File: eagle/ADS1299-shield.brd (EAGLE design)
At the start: 101.6 x 53.3 mm, 125 parts, among them IC1 ADS1299IPAG, IC2 TPS72325DBVT, IC3 TPS73225DBVT, IC5 24AA256UID, IC6 TPS604XXDBV, IC7 OPA376DBV, IC8 OPA376DBV, J8 Electrode Connector, U2 TXB0108PWR, U3 TXB0108PWR

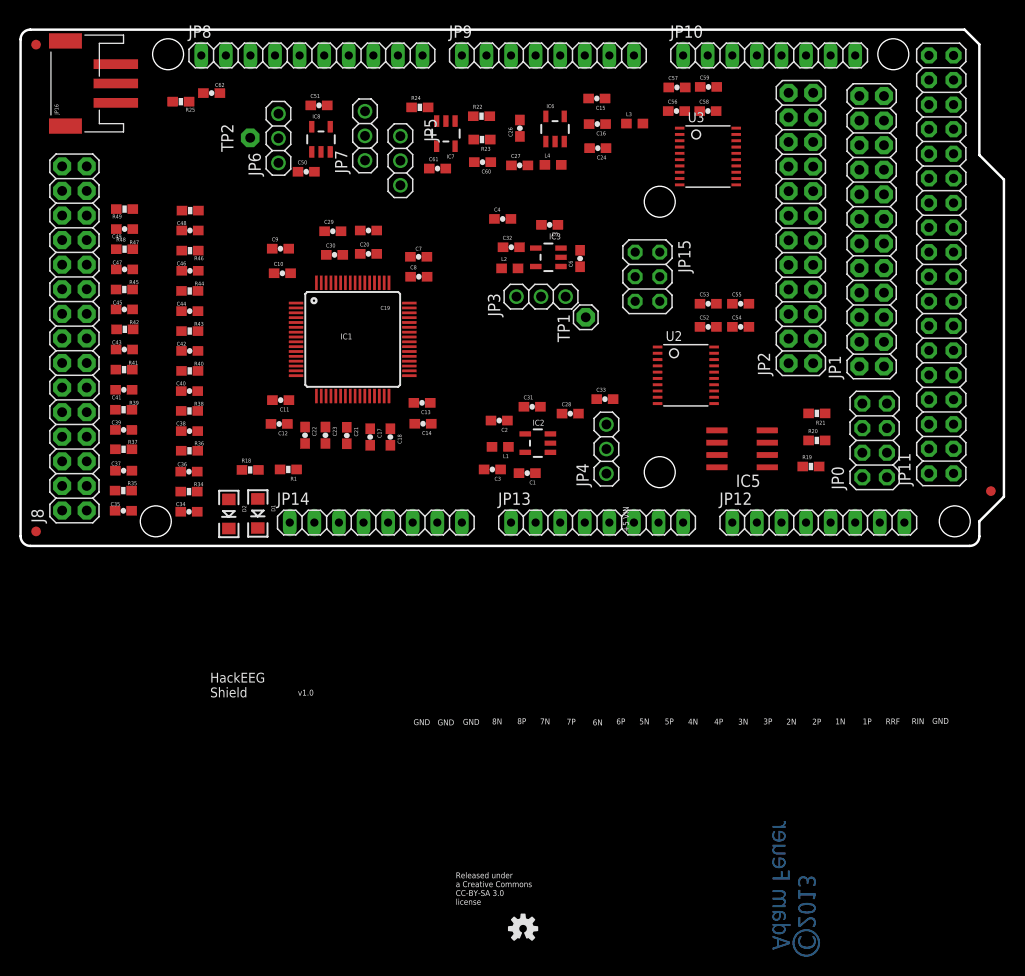
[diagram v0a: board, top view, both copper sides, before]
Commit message: new component arrangement - AIN block neat; configuration blocks moved to make more space for routing
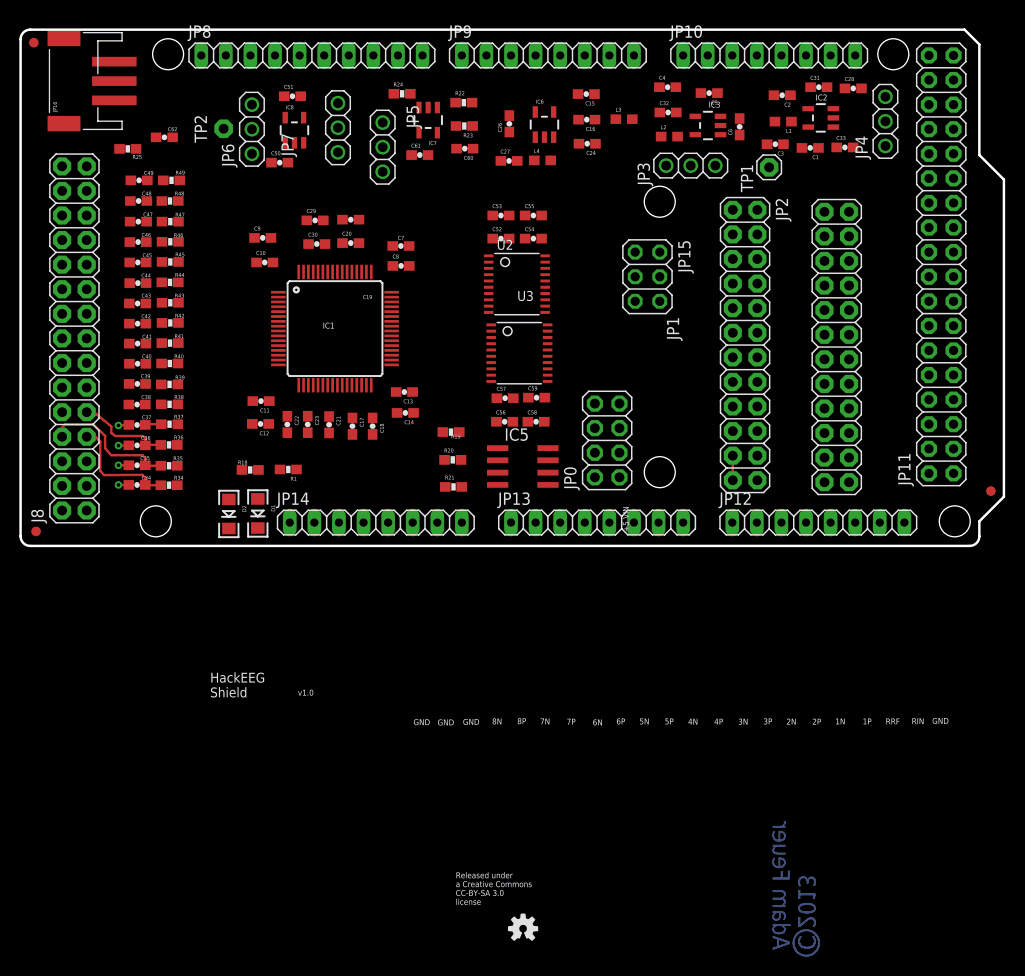
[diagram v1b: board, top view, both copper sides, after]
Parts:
- moved C2 44.5 mm to (78.8, 46.7)
- moved C28 44.5 mm to (86.2, 47.4)
- moved C3 44.5 mm to (78.1, 41.6)
- moved C1 44.5 mm to (81.7, 41.2)
- moved IC2 44.5 mm to (82.8, 44.3)
- moved L1 44.5 mm to (78.9, 44.0)
- moved JP4 44.5 mm to (89.5, 44.0)
- moved C31 44.4 mm to (82.6, 47.5)
- moved R21 38.3 mm to (44.9, 6.22), turned to 0 degrees
- moved R20 37.7 mm to (44.8, 9.02)
- moved R19 37.4 mm to (44.6, 11.9), turned to 180 degrees
- moved C59 36.7 mm to (53.4, 15.4)
- moved C56 36.7 mm to (50.1, 13.0)
- moved C57 36.7 mm to (50.2, 15.4)
- moved C58 36.7 mm to (53.4, 13.0)
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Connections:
- new net N$551: JP2.1, JP2.3
- new net N$552: JP2.2
- new net N$553: JP2.4
- net !ADC_RESET_0: no longer JP2.22
- net !ADC_RESET_1: no longer JP2.24
- net !ADS_SPI_CS: now also U2.15; no longer U2.18
- net !RESET: no longer JP2.21, JP2.23
- net !SPI_CS: now also U2.6; no longer U2.3
- net ADS_CLKSEL: now also U2.20; no longer U2.14
- net ADS_DRDY: now also U2.18; no longer U2.20
- net ADS_SPI_CLK: now also U2.16; no longer U2.17
- net ADS_SPI_IN: now also JP2.21, JP2.23, U2.14; no longer JP2.1, JP2.3, U2.16
- net ADS_SPI_OUT: now also U2.17; no longer U2.15
- net CLKSEL: now also U2.1; no longer U2.7
- net DRDY: now also U2.3; no longer U2.1
- net SPI0_MOSI: now also JP2.22; no longer JP2.2
- net SPI0_SCK: now also JP2.12; no longer JP2.10
- net SPI_CLK: now also U2.5; no longer U2.4
- net SPI_IN: now also U2.7; no longer U2.5
- net SPI_OUT: now also U2.4; no longer U2.6
- net USART1_MOSI: now also JP2.24; no longer JP2.4
- net USART1_SCK: now also JP2.10; no longer JP2.12
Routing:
- net AIN1N: track 0.00 -> 14.6 mm
- net AIN1P: track 0.00 -> 12.0 mm
- net AIN2P: track 0.00 -> 11.2 mm
- net AGND: track 0.00 -> 10.5 mm, vias 0 -> 4
- net ADS_SPI_IN: track 0.00 -> 2.54 mm
- net AIN2N: track 0.00 -> 2.05 mm
- added copper zone on layer 2, net AGND
- added copper zone on layer 15, net DVDD
- removed copper zone on layer 2, net N$22
- removed copper zone on layer 15, net N$25

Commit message: AIN block fully routed
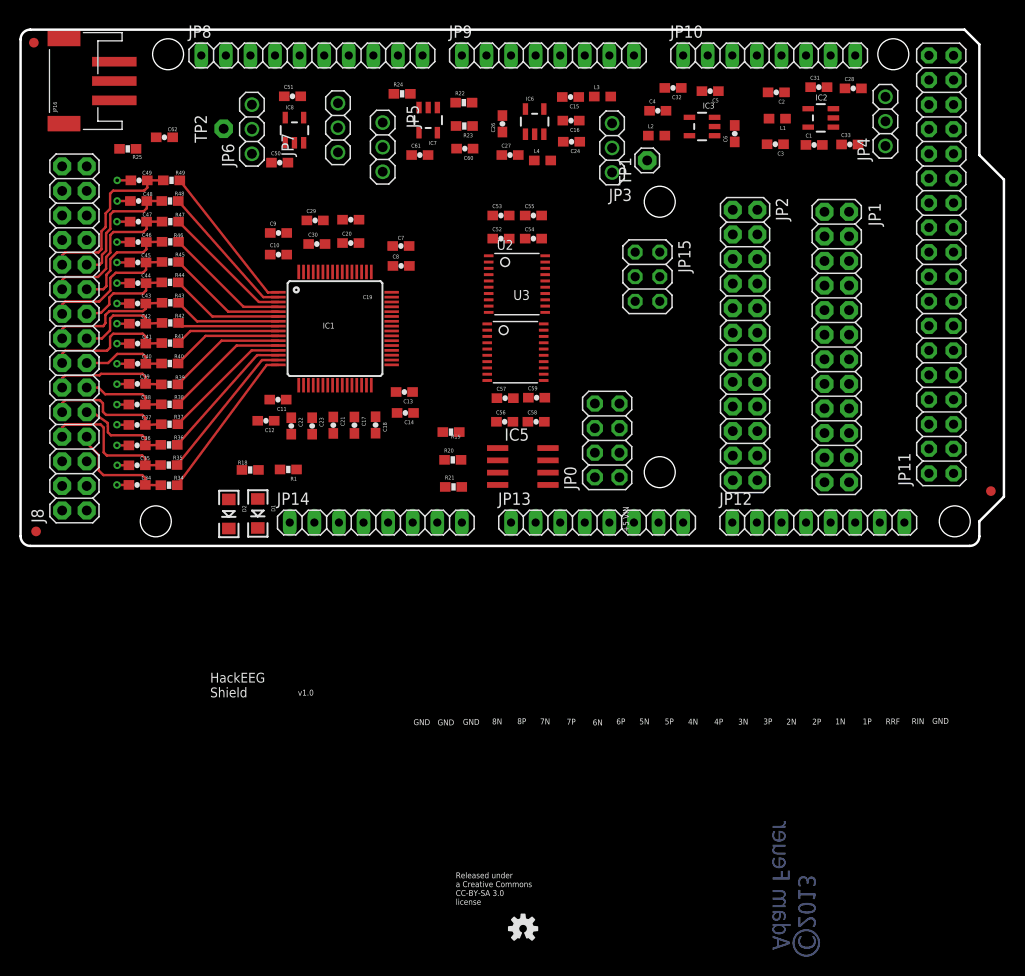
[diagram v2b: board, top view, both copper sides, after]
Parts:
- moved TP1 12.6 mm to (64.9, 40.0)
- moved JP3 8.33 mm to (61.2, 41.2), turned to 90 degrees
- moved L3 3.23 mm to (60.2, 46.6)
- moved C4 2.64 mm to (66.0, 45.1)
- moved C32 2.59 mm to (67.5, 47.4), turned to 180 degrees
- moved C11 1.76 mm to (26.7, 15.2)
- moved C9 1.70 mm to (26.8, 32.5)
- moved C15 1.65 mm to (56.9, 46.5)
- moved C10 1.64 mm to (26.8, 30.2)
- moved C24 1.64 mm to (57.0, 41.9)
- moved C16 1.63 mm to (57.0, 44.1)
- moved L2 1.32 mm to (65.8, 42.5)
- moved IC6 1.06 mm to (53.2, 44.0)
- moved C6 0.87 mm to (73.9, 42.7)
- moved C26 0.71 mm to (49.9, 43.7)
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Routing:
- net AGND: track 10.5 -> 52.5 mm, vias 4 -> 16
- net AIN8N: track 0.00 -> 17.9 mm
- net IN1P: track 0.00 -> 16.7 mm
- net AIN7N: track 0.00 -> 16.0 mm
- net IN8N: track 0.00 -> 15.8 mm
- net IN1N: track 0.00 -> 15.6 mm
- net IN8P: track 0.00 -> 14.8 mm
- net IN2P: track 0.00 -> 14.6 mm
- net AIN6N: track 0.00 -> 14.3 mm
- net IN7N: track 0.00 -> 13.8 mm
- net AIN4N: track 0.00 -> 13.6 mm
- net IN2N: track 0.00 -> 13.6 mm
- net AIN8P: track 0.00 -> 13.3 mm
- net AIN5N: track 0.00 -> 13.2 mm
- net IN7P: track 0.00 -> 13.1 mm
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
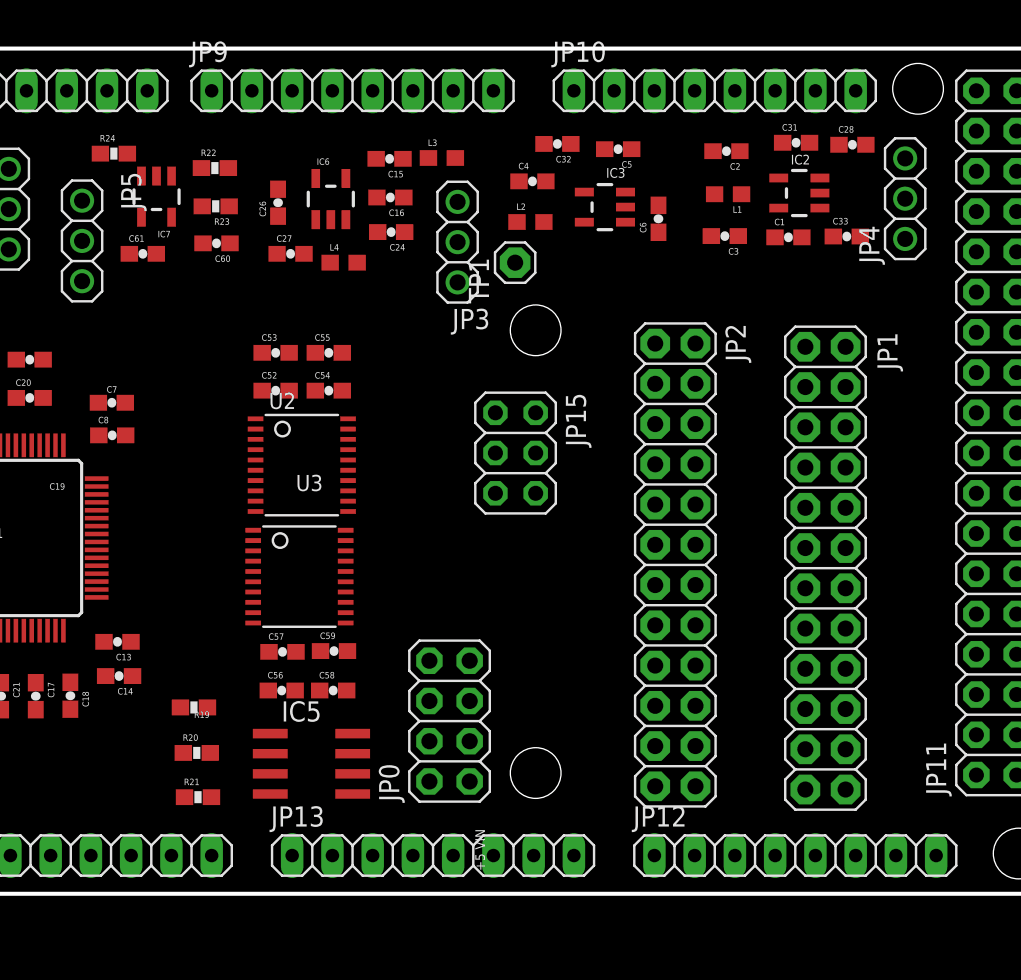
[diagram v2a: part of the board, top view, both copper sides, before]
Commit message: updated 2X10 and 2X12 headers to use smaller pads that can route 2 8mil traces between them; routed SPI MOSI, MISO, and CLK to header pins
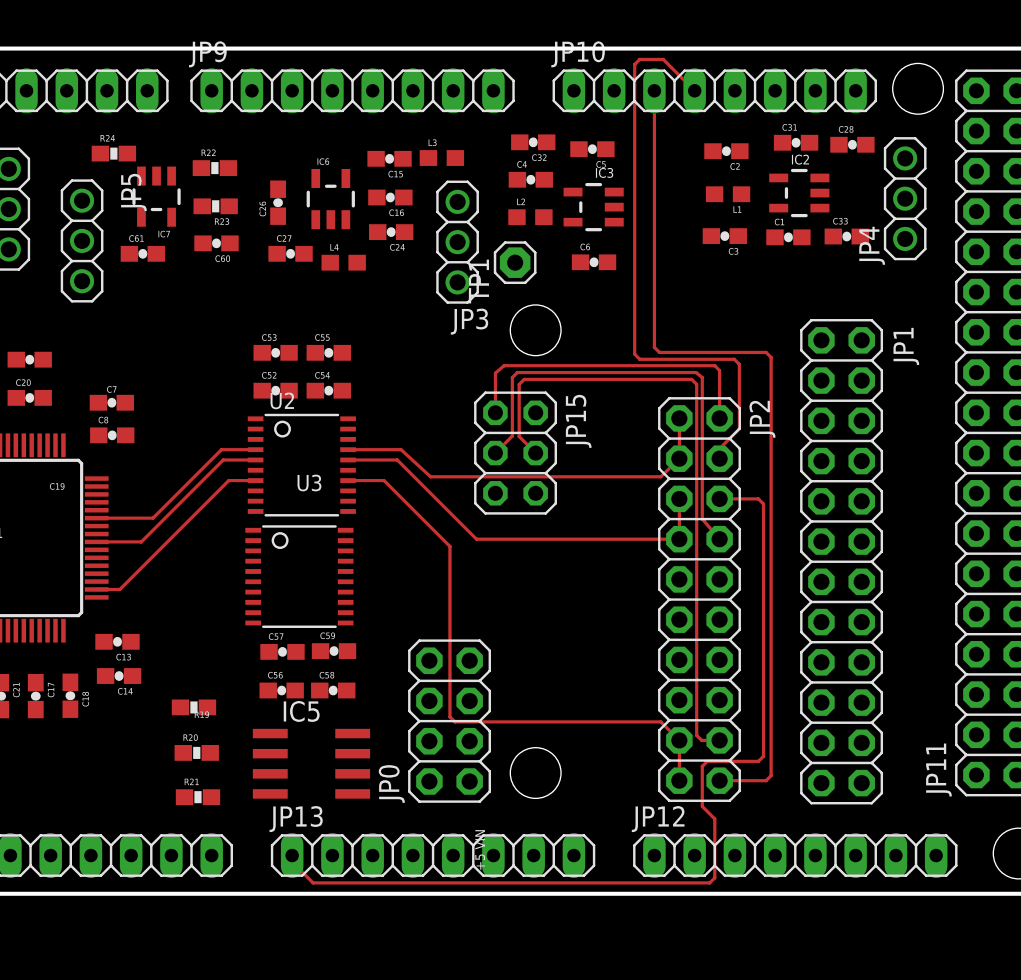
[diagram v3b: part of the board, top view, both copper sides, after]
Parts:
- JP2: value CONFIG2 -> CONFIG3; device pin-headers:2X12 -> headers:2X10
- moved JP2 5.33 mm to (76.5, 18.7)
- moved C6 4.90 mm to (69.8, 40.0), turned to 0 degrees
- moved C5 1.63 mm to (69.7, 47.1)
- moved C32 1.53 mm to (66.0, 47.5)
- moved JP1 1.09 mm to (88.0, 19.8)
- moved IC3 0.71 mm to (69.8, 43.5)
- moved L2 0.30 mm to (65.8, 42.8)
- moved C4 0.14 mm to (65.9, 45.2)
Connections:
- removed net N$551: JP2.1, JP2.3
- removed net N$552: JP2.2
- removed net N$553: JP2.4
- net !ADC_CS_0: now also JP2.10; no longer JP2.14
- net !ADC_CS_1: now also JP2.12; no longer JP2.16
- net !ADC_CS_2: now also JP2.14; no longer JP2.18
- net !ADC_CS_3: now also JP2.16; no longer JP2.20
- net !ADS_SPI_CS: now also JP2.11, JP2.9; no longer JP2.17, JP2.19
- net ADS_SPI_CLK: now also JP2.5, JP2.7; no longer JP2.11, JP2.9
- net ADS_SPI_IN: now also JP2.17, JP2.19; no longer JP2.21, JP2.23
- net ADS_SPI_OUT: now also JP2.1, JP2.3; no longer JP2.5, JP2.7
- net SPI0_MISO: now also JP2.2; no longer JP2.6
- net SPI0_MOSI: now also JP2.18; no longer JP2.22
- net SPI0_SCK: now also JP2.8; no longer JP2.12
- net USART1_MISO: now also JP2.4; no longer JP2.8
- net USART1_MOSI: now also JP2.20; no longer JP2.24
- net USART1_SCK: now also JP2.6; no longer JP2.10
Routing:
- net USART1_SCK: track 0.00 -> 58.1 mm
- net USART1_MOSI: track 0.00 -> 53.6 mm
- net SPI0_MOSI: track 0.00 -> 40.0 mm
- net ADS_SPI_IN: track 0.00 -> 36.5 mm
- net USART1_MISO: track 0.00 -> 36.4 mm
- net SPI0_SCK: track 0.00 -> 28.0 mm
- net ADS_SPI_CLK: track 0.00 -> 25.5 mm
- net ADS_SPI_OUT: track 0.00 -> 24.6 mm
- net SPI0_MISO: track 0.00 -> 20.0 mm
- net SPI_IN: track 0.00 -> 12.9 mm
- net SPI_CLK: track 0.00 -> 12.2 mm
- net SPI_OUT: track 0.00 -> 11.8 mm

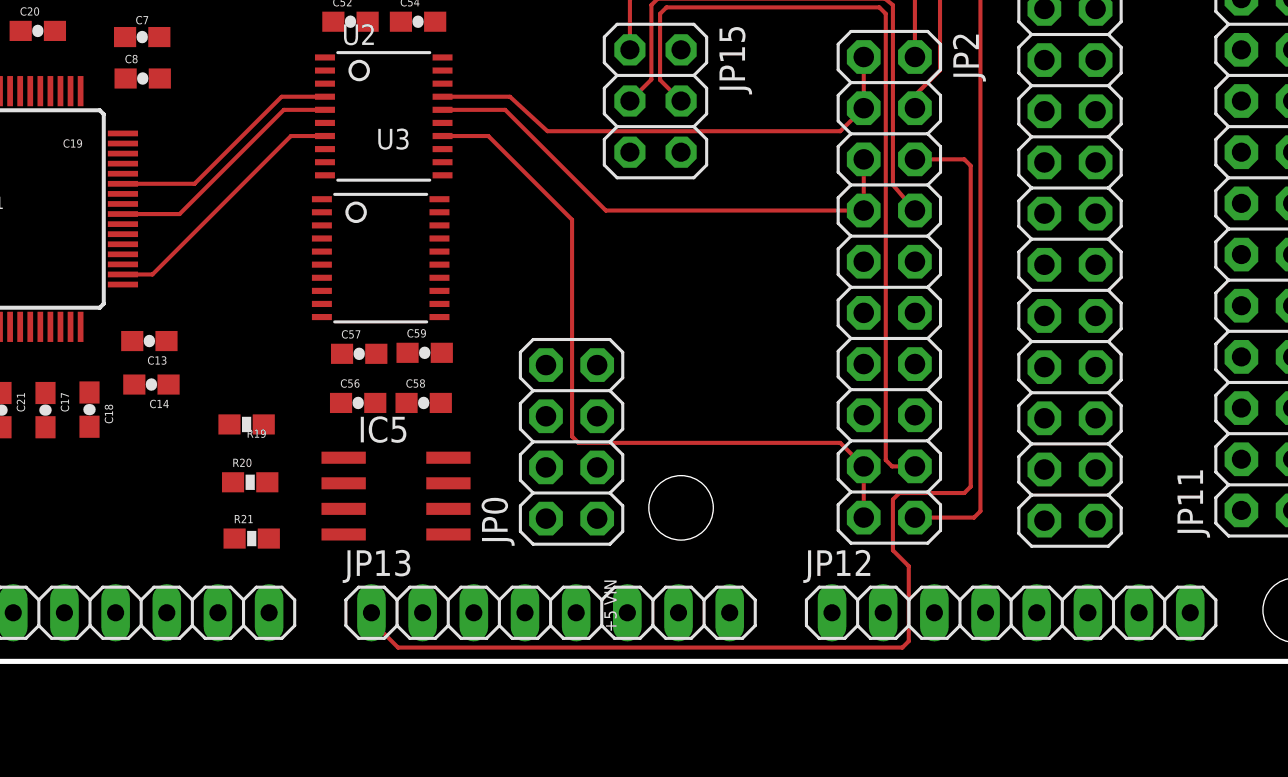
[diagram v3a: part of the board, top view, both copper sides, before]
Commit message: fully routed ADS1299 CLK signal to connector pins
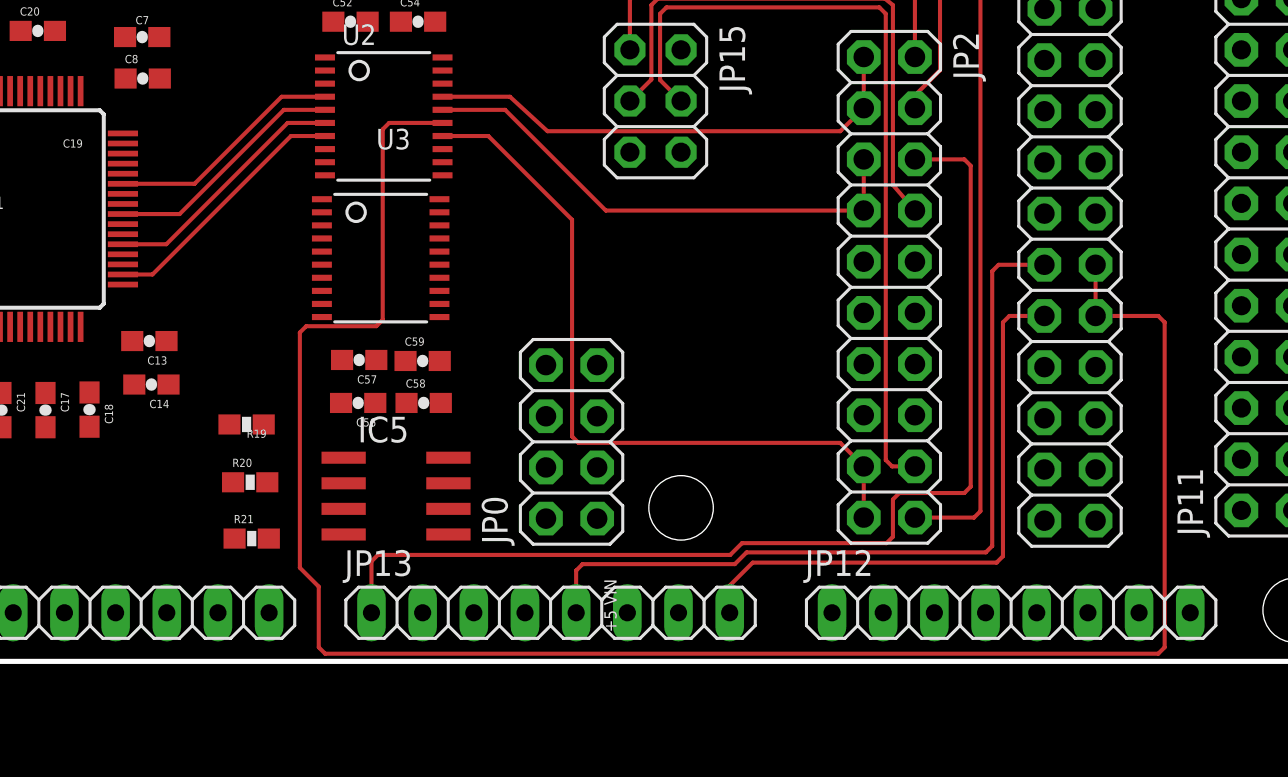
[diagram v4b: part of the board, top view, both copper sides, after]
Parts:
- moved C59 0.42 mm to (53.3, 15.0)
- moved C57 0.30 mm to (50.2, 15.1), turned to 180 degrees
- turned C56 to 180 degrees
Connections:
- net !ADS_SPI_CS: now also U3.14; no longer U2.15
- net !SPI_CS: now also U3.7; no longer U2.6
- net ADS_CLK: now also U2.15; no longer U3.14
- net CLK: now also U2.6; no longer U3.7
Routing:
- net ADS_CLK: track 0.00 -> 97.4 mm
- net ADC_CLK_1: track 0.00 -> 39.6 mm
- net ADC_CLK_0: track 0.00 -> 29.3 mm
- net CLK: track 0.00 -> 12.5 mm
- net USART1_SCK: track 58.1 -> 53.7 mm
